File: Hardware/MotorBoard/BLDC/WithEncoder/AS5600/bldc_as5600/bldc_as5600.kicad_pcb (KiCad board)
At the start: 2 copper layers, 66.8 x 65.6 mm, 47 parts, among them CN10 PR5L4015-5P-C-F, CN11 PR5L4015-5P-C-F, CN7 PR5L4015-5P-C-F, CN8 PR5L4015-5P-C-F, CN9 PR5L4015-5P-C-F, U1 AS5600-ASOT, U35 PR5L5015-5P-C-H, U36 PR5L5015-5P-C-H, U37 PR5L5015-5P-C-H, U38 PR5L5015-5P-C-H, U39 PR5L5015-5P-C-H

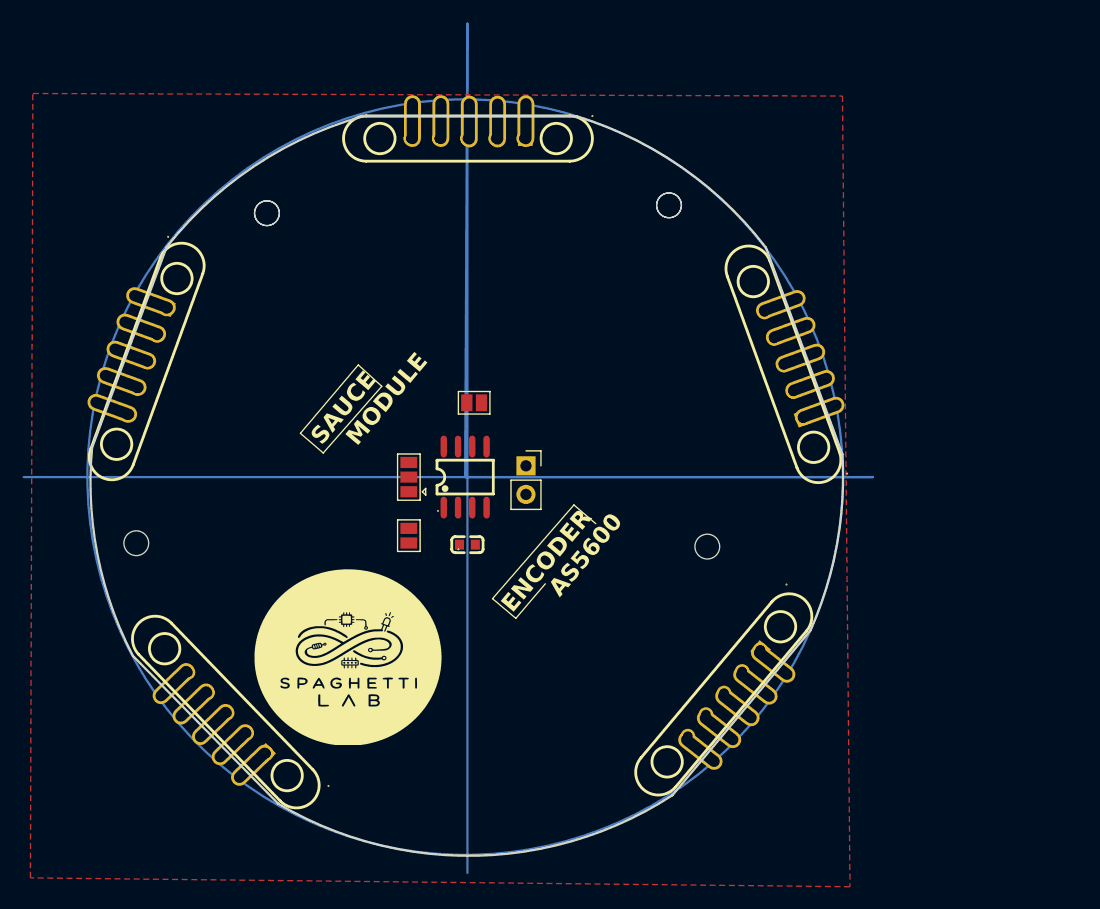
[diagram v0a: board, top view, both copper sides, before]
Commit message: Placed holes for motor mount
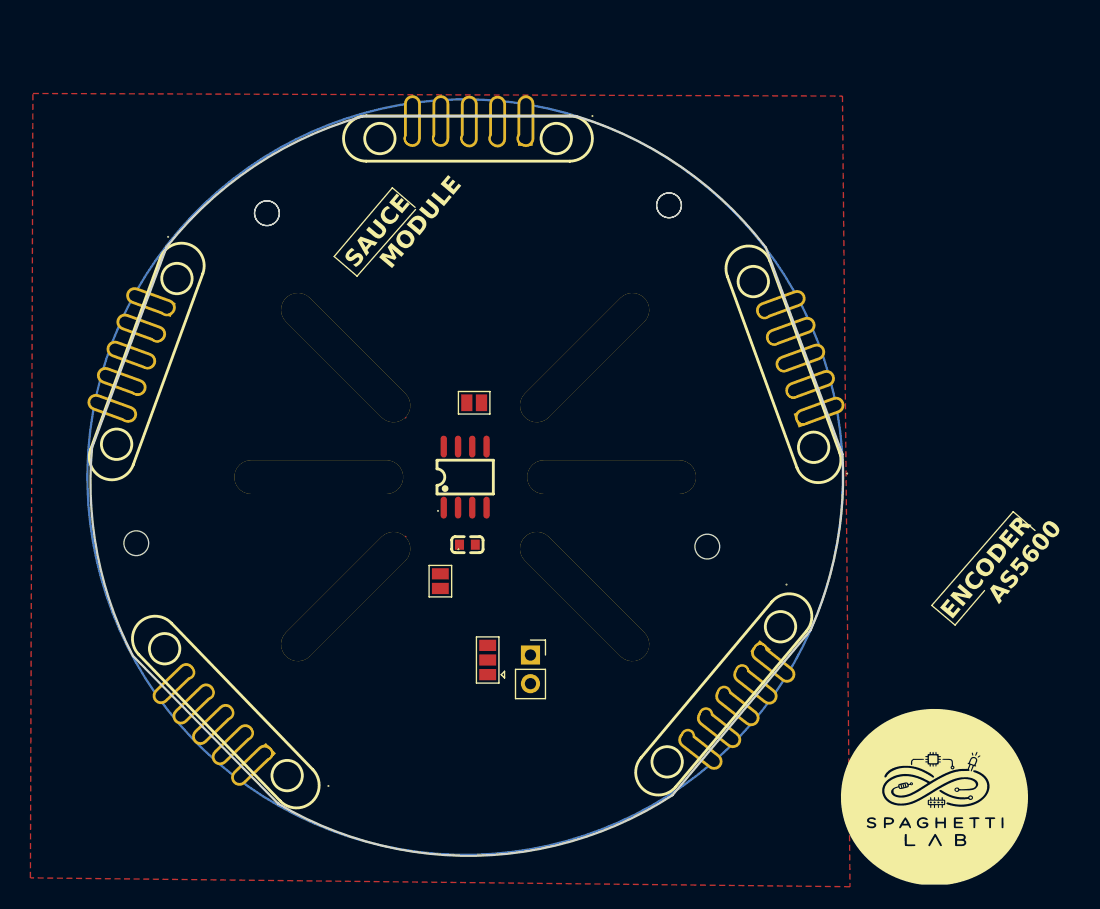
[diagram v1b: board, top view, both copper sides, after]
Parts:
- added ?: , , F.Cu at (170.0, 100.9)
- added ?: , , F.Cu at (170.0, 122.1)
- added ?: , , F.Cu at (193.6, 111.5)
- added ?: , , F.Cu at (191.2, 100.9)
- added ?: , , F.Cu at (191.2, 122.1)
- added ?: , , F.Cu at (167.6, 111.5)
- moved JP1 17.7 mm to (182.6, 127.7)
- moved JP4 16.8 mm to (186.4, 127.3)
- moved JP3 4.92 mm to (178.4, 120.7)

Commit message: Done layout for as5600 encoder board
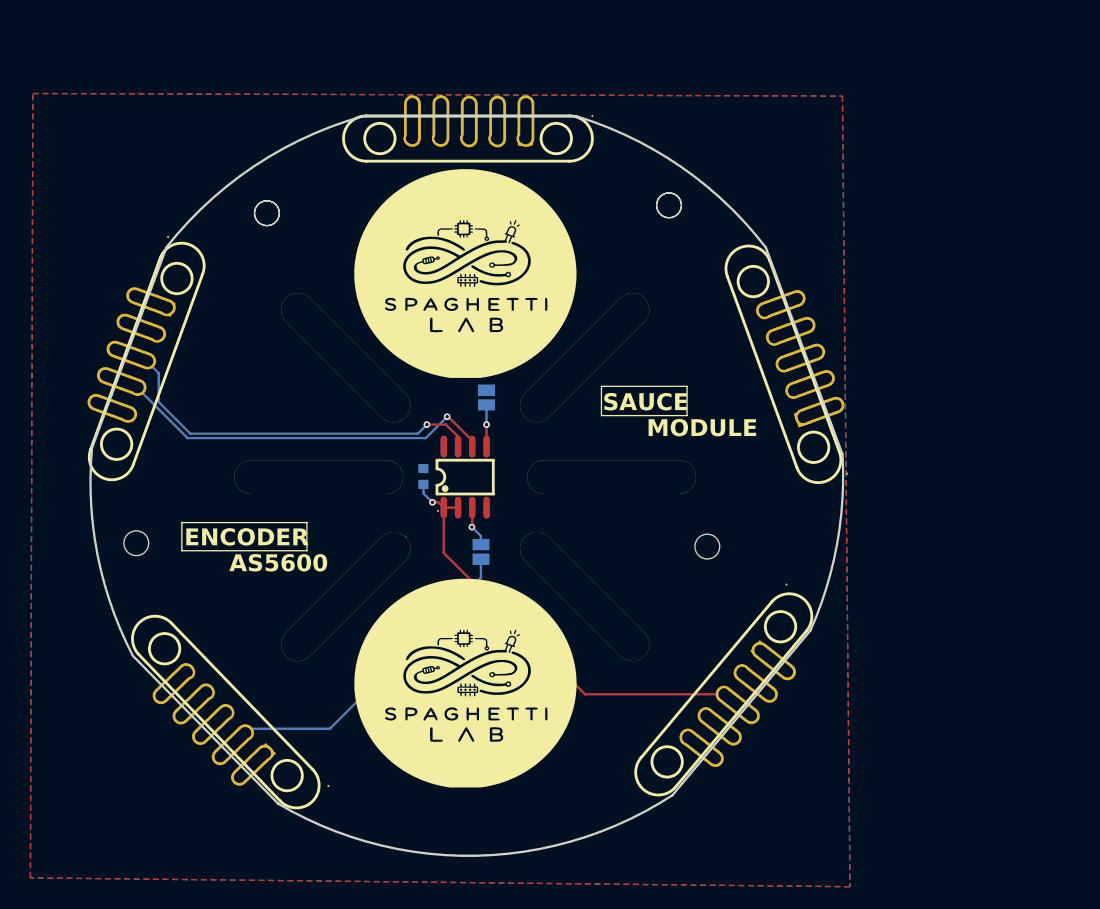
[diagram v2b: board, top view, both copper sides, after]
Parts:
- removed JP1: ENC_DIR, Jumper:SolderJumper-3_P1.3mm_Open_Pad1.0x1.5mm
- removed JP3: VLOGIC23V3, Jumper:SolderJumper-2_P1.3mm_Open_Pad1.0x1.5mm
- C1, JP2: moved to B.Cu
- JP4: value VLOGIC23V3 -> ENC_PGO; footprint Connector_PinSocket_2.54mm:PinSocket_1x02_P2.54mm_Vertical -> Jumper:SolderJumper-2_P1.3mm_Open_Pad1.0x1.5mm; moved to B.Cu
- moved JP4 10.2 mm to (182.0, 118.1), turned to -90 degrees
- moved ? 10.0 mm to (214.8, 131.7)
- moved C1 7.21 mm to (176.9, 111.4), turned to 90 degrees
- moved JP2 1.19 mm to (182.5, 104.4), turned to 90 degrees
- moved ? 0.27 mm to (201.6, 135.5)
- moved ? 0.23 mm to (203.2, 133.6)
- moved ? 0.22 mm to (208.0, 127.8)
- moved ? 0.16 mm to (206.4, 129.8)
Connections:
- CN11 pad 3: VLOGIC -> +3.3V
- U1 pad 8: Net-(JP1-C) -> GND
- U39 pad 3: VLOGIC -> +3.3V
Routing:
- net +3.3V: track 0.00 -> 38.5 mm, vias 0 -> 1
- net ENC_SDA: track 0.00 -> 33.9 mm, vias 0 -> 1
- net ENC_SCL: track 0.00 -> 33.4 mm, vias 0 -> 1
- net /FLEX3: track 0.00 -> 28.2 mm
- net Net-(JP2-A): track 0.00 -> 3.70 mm, vias 0 -> 1
- net ENC_AOUT: track 0.00 -> 3.62 mm, vias 0 -> 1
- added copper zone on B.Cu, net GND

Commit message: Added JST for UART to display module
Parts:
- added J1: Conn_01x04_Socket, Connector_JST:JST_GH_SM04B-GHS-TB_1x04-1MP_P1.25mm_Horizontal, F.Cu at (175.3, 140.6)
- added J2: Conn_01x04_Socket, Connector_JST:JST_GH_SM04B-GHS-TB_1x04-1MP_P1.25mm_Horizontal, F.Cu at (188.8, 140.0)
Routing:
- net /~{RESET}: track 0.00 -> 95.9 mm, vias 0 -> 1
- net +3.3V: track 38.5 -> 69.9 mm
- net /ID: track 0.00 -> 17.3 mm

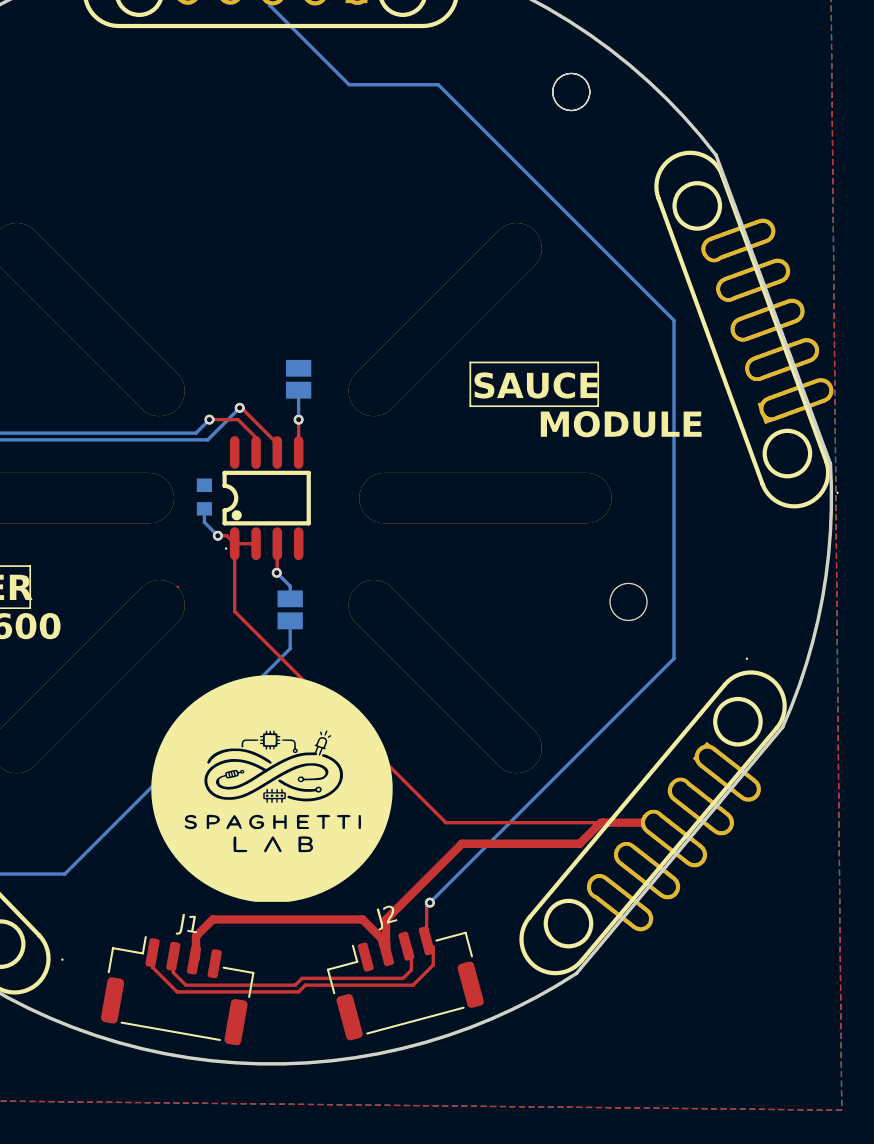
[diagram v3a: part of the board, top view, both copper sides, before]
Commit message: removed a jst in encoder board
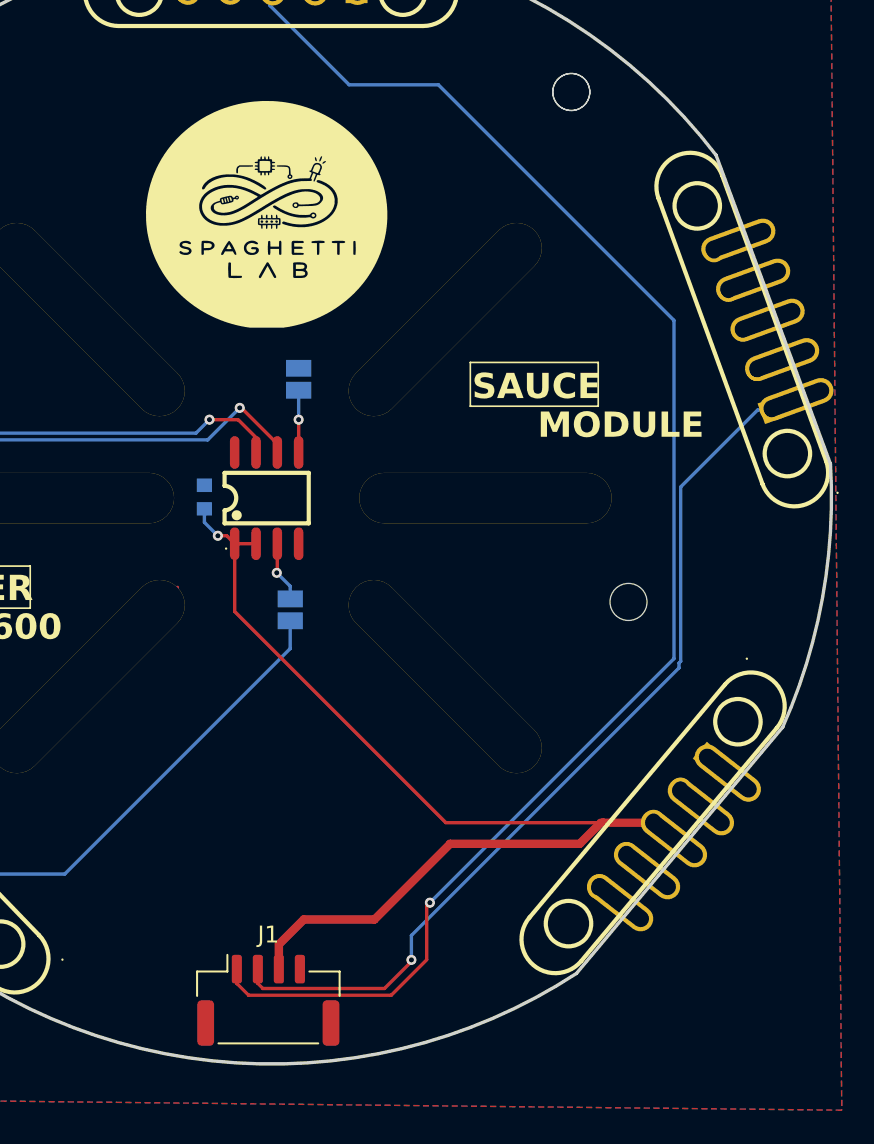
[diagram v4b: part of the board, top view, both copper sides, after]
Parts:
- removed J2: Conn_01x04_Socket, Connector_JST:JST_GH_SM04B-GHS-TB_1x04-1MP_P1.25mm_Horizontal
- moved J1 5.40 mm to (180.7, 141.3), turned to 0 degrees
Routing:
- net /ID: track 17.3 -> 52.9 mm, vias 0 -> 1
- net +3.3V: track 69.9 -> 62.2 mm
- net /~{RESET}: track 95.9 -> 89.9 mm
